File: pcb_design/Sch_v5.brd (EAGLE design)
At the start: 85.1 x 49.5 mm, 32 parts

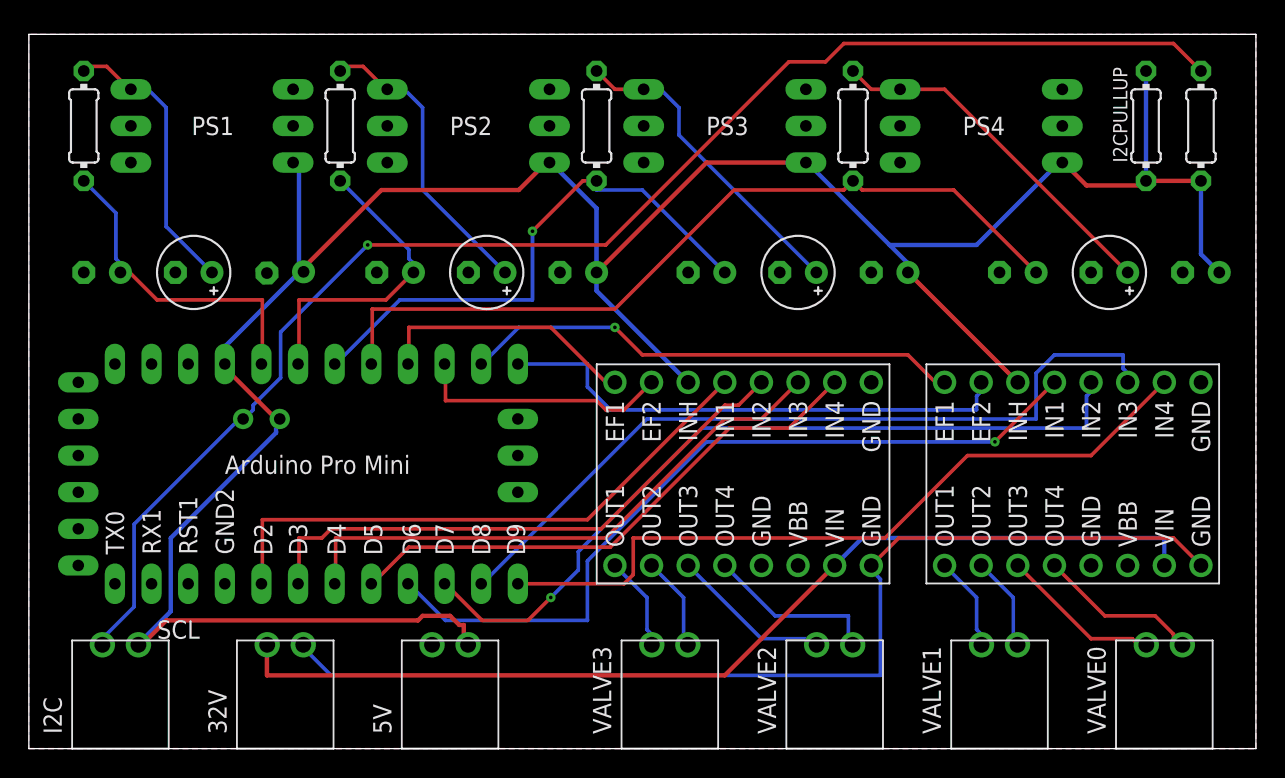
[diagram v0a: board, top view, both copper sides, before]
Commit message: updated to v5. Cleaned up schematic a bit. Still need to fix I2C, flipped pins, etc.
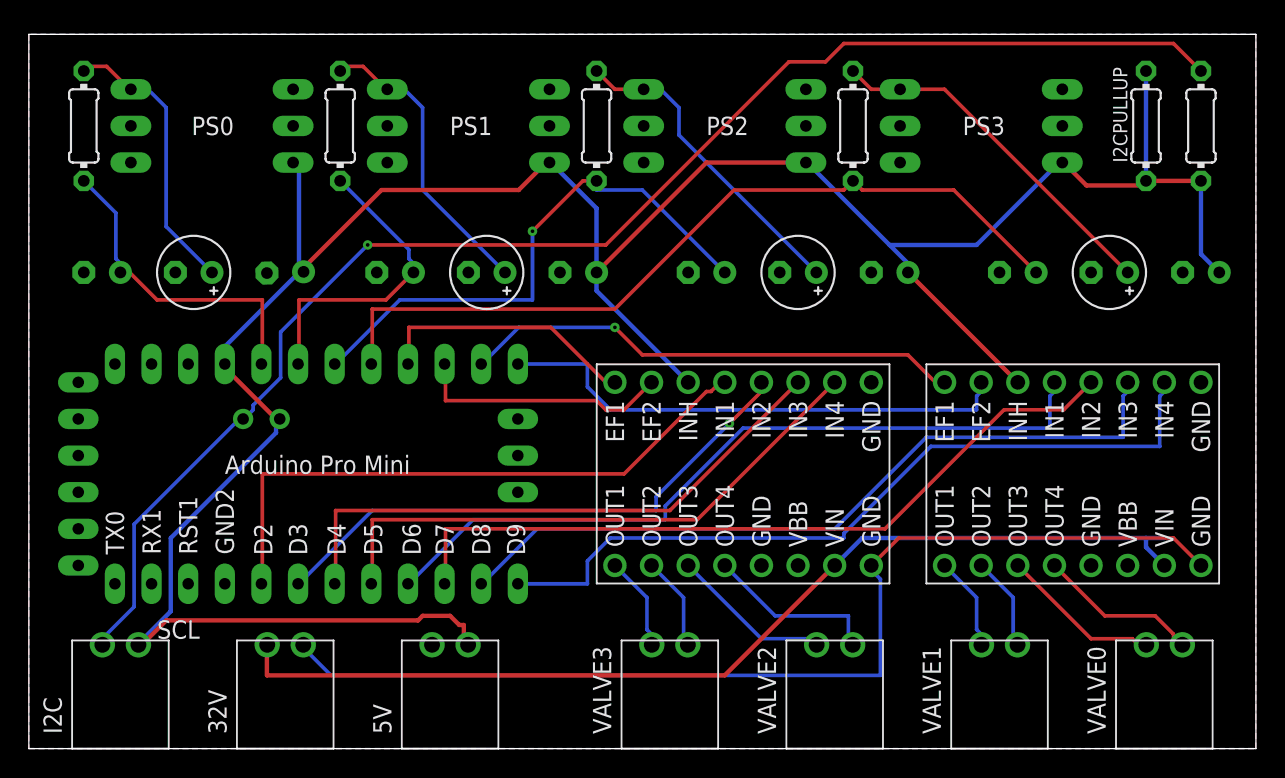
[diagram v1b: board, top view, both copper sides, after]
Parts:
- removed PS4: (no value), RAD_2:ABPDRNN100PGAA5
- added PS0: (no value), RAD_2:ABPDRNN100PGAA5
- moved PS1 17.8 mm to (6.35, -3.81)
- moved PS2 17.8 mm to (24.1, -3.81)
- moved PS3 17.8 mm to (41.9, -3.81)
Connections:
- net N$10 renamed A1
- net N$11 renamed A2
- net N$12 renamed A3
- net N$17 renamed D2
- net N$18 renamed D3
- net N$19 renamed D4
- net N$20 renamed D5
- net N$23 renamed D6
- net N$24 renamed D7
- net N$25 renamed D8
- net N$26 renamed D9
- net N$9 renamed A0
- net GND: now also PS0.1; no longer PS4.1
- net N$1: now also PS0.3; no longer PS1.3
- net N$2: now also PS1.3; no longer PS2.3
- net N$3: now also PS2.3; no longer PS3.3
- net N$4: now also PS3.3; no longer PS4.3
- net VDD: now also PS0.6; no longer PS4.6
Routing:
- net D5: track 37.9 -> 40.5 mm
- net D8: track 55.0 -> 52.7 mm
- net D7: track 55.1 -> 52.8 mm, vias 1 -> 0
- net D6: track 55.1 -> 52.8 mm, vias 1 -> 0
- net D9: track 52.1 -> 54.2 mm
- net D2: track 40.5 -> 42.4 mm
- net D4: track 39.8 -> 40.9 mm
- net D3: track 39.8 -> 38.8 mm, vias 0 -> 1
- net VIN: track 70.2 -> 70.7 mm

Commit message: Fixed I2C traces, changed power on arduino from VCC pin to Raw, updated silkscreen
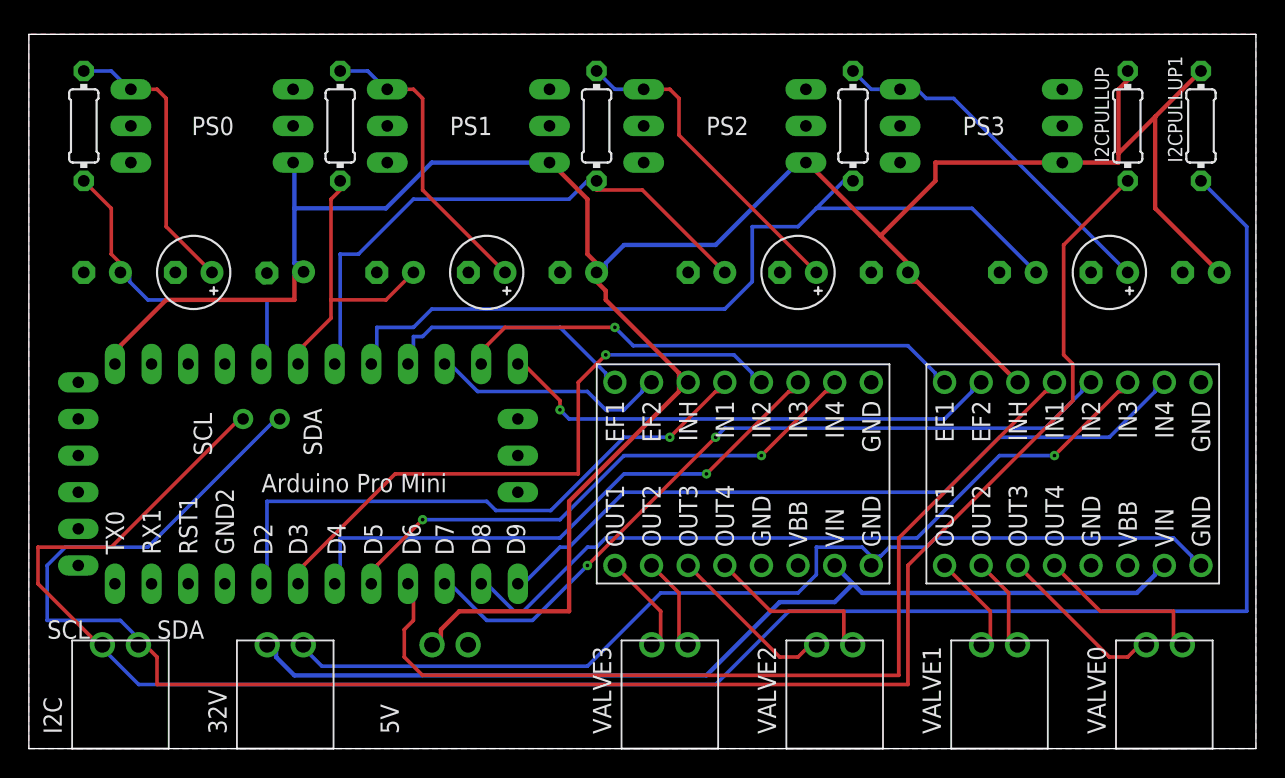
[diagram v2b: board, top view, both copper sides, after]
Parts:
- moved I2CPULLUP 1.27 mm to (52.1, -3.81)
- flipped 5V to the bottom
- turned I2CPULLUP1 to 90 degrees
- renumbered R5 to I2CPULLUP1
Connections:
- new net N$9: I2C.2, I2CPULLUP.1, U$1.A4
- net VDD: now also U$1.RAW; no longer I2C.2, I2CPULLUP.1, U$1.A4, U$1.VCC
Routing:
- net N$9: track 0.00 -> 129.4 mm
- net N$21: track 100.0 -> 140.9 mm, vias 1 -> 0
- net D6: track 52.8 -> 65.7 mm
- net D3: track 38.8 -> 44.3 mm
- net VDD: track 185.7 -> 181.1 mm
- net A3: track 56.2 -> 59.5 mm
- net D9: track 54.2 -> 51.0 mm
- net GND2: track 73.3 -> 70.4 mm
- net A2: track 38.1 -> 39.8 mm, vias 1 -> 0
- net D5: track 40.5 -> 39.0 mm, vias 0 -> 2
- net VIN: track 70.7 -> 69.3 mm
- net N$7: track 11.2 -> 12.5 mm
- net E3: track 34.8 -> 35.9 mm
- net E2: track 17.9 -> 16.8 mm
- net A1: track 21.7 -> 20.6 mm
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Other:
- board text added: "SDA"
